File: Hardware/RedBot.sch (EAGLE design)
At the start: 39 parts, among them U2 TB6612FNG, U3 MIC5219 5V

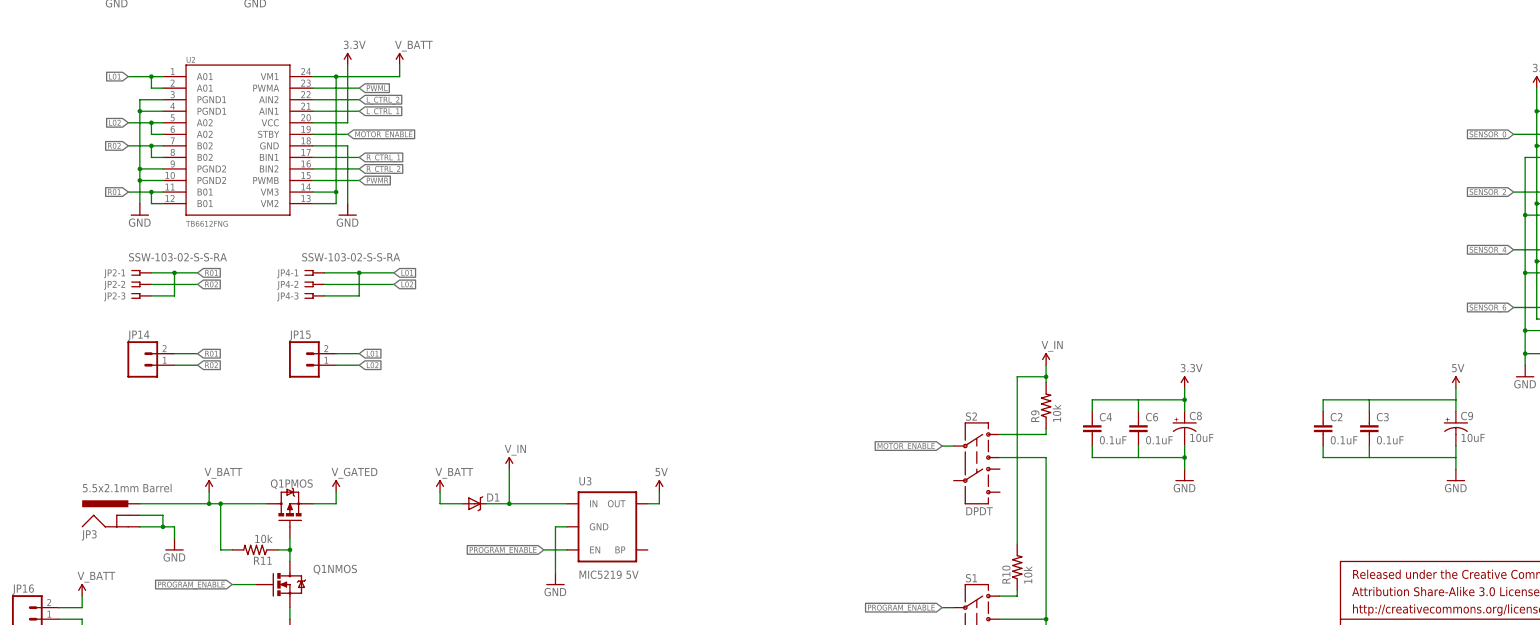
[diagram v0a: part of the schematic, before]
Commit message: Updated board with new power jack. Started routing. Added BOM
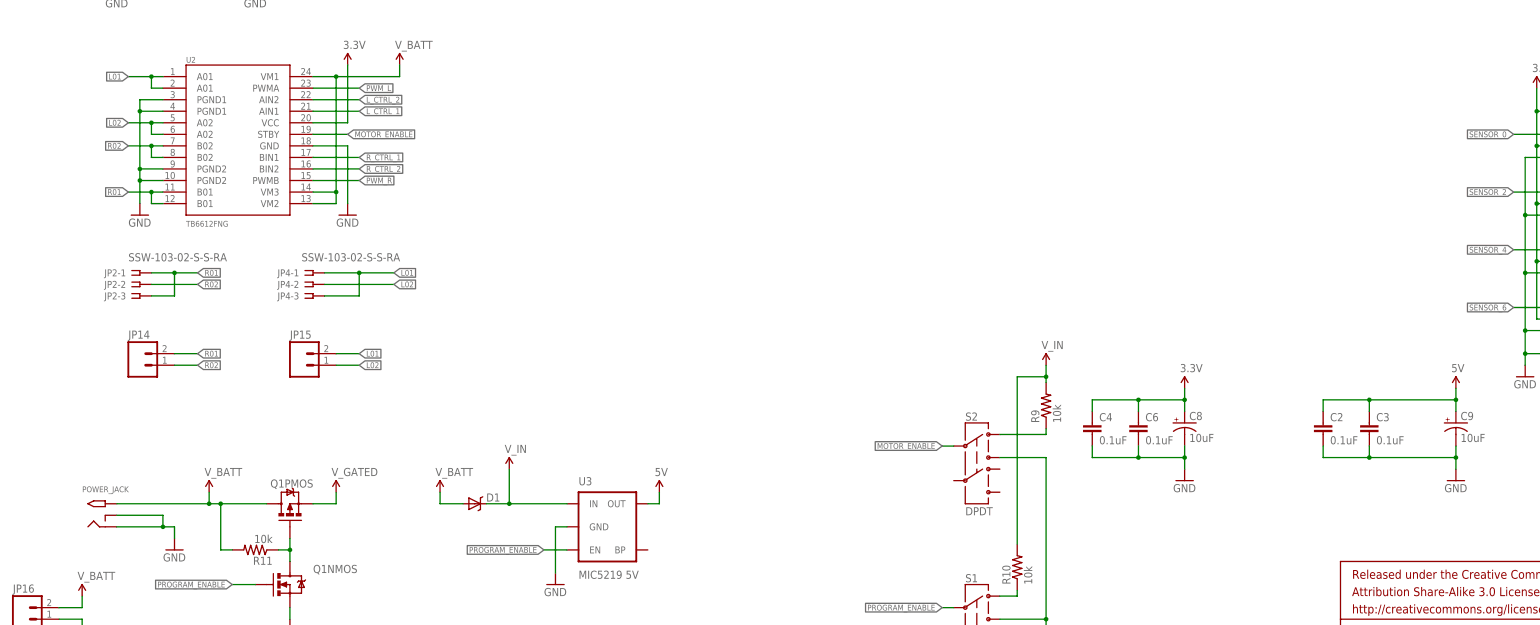
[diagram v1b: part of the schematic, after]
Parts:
- removed JP3: 5.5x2.1mm Barrel, SparkFun-Connectors:POWER_JACKSMD
- added POWER_JACK: 2.1MMJACKTHM, adafruit:2.1MMJACKTHM
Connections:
- removed net PWML: U2.PWMA
- removed net PWMR: U2.PWMB
- net GND: now also POWER_JACK.RING, POWER_JACK.RING_SW; no longer JP3.GND, JP3.GNDBREAK
- net PWM_L: now also U2.PWMA
- net PWM_R: now also U2.PWMB
- net V_BATT: now also POWER_JACK.TIP; no longer JP3.PWR
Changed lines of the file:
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@@
 <setting verticaltext="up"/>
 </settings>
-<grid distance="0.1" unitdist="inch" unit="inch" style="lines" multiple="1" display="no" altdistance="0.01" altunitdist="inch" altunit="inch"/>
+<grid distance="0.05" unitdist="inch" unit="inch" style="lines" multiple="1" display="yes" altdistance="0.005" altunitdist="inch" altunit="inch"/>
 <layers>
 <layer number="1" name="Top" color="4" fill="1" visible="no" active="no"/>
@@
 <layer number="54" name="bGND_GNDA" color="1" fill="9" visible="no" active="no"/>
 <layer number="56" name="wert" color="7" fill="1" visible="no" active="no"/>
+<layer number="57" name="tCAD" color="7" fill="1" visible="no" active="no"/>
 <layer number="59" name="tCarbon" color="7" fill="1" visible="no" active="no"/>
 <layer number="60" name="bCarbon" color="7" fill="1" visible="no" active="no"/>
@@
 <layer number="111" name="Design_Info" color="7" fill="1" visible="yes" active="yes"/>
 <layer number="112" name="CC430_Restrict" color="7" fill="1" visible="yes" active="yes"/>
+<layer number="113" name="IDFDebug" color="4" fill="1" visible="yes" active="yes"/>
 <layer number="116" name="Patch_BOT" color="9" fill="4" visible="no" active="yes"/>
 <layer number="121" name="_tsilk" color="7" fill="1" visible="no" active="yes"/>
@@
 <layer number="125" name="_tNames" color="7" fill="1" visible="no" active="yes"/>
 <layer number="126" name="_bNames" color="7" fill="1" visible="yes" active="yes"/>
+<layer number="127" name="_tValues" color="7" fill="1" visible="yes" active="yes"/>
+<layer number="128" name="_bValues" color="7" fill="1" visible="yes" active="yes"/>
 <layer number="129" name="Mask" color="7" fill="1" visible="yes" active="yes"/>
 <layer number="131" name="tAdjust" color="7" fill="1" visible="yes" active="yes"/>
 <layer number="132" name="bAdjust" color="7" fill="1" visible="yes" active="yes"/>
 <layer number="144" name="Drill_legend" color="7" fill="1" visible="no" active="yes"/>
+<layer number="150" name="Notes" color="7" fill="1" visible="no" active="yes"/>
 <layer number="151" name="HeatSink" color="7" fill="1" visible="no" active="yes"/>
+<layer number="152" name="_bDocu" color="7" fill="1" visible="yes" active="yes"/>
+<layer number="153" name="FabDoc1" color="6" fill="1" visible="no" active="no"/>
+<layer number="154" name="FabDoc2" color="2" fill="1" visible="no" active="no"/>
+<layer number="155" name="FabDoc3" color="7" fill="15" visible="no" active="no"/>
 <layer number="199" name="Contour" color="7" fill="1" visible="yes" active="yes"/>
 <layer number="200" name="200bmp" color="1" fill="10" visible="no" active="yes"/>
@@
 <layer number="223" name="223bmp" color="24" fill="1" visible="no" active="no"/>
 <layer number="224" name="224bmp" color="25" fill="1" visible="no" active="no"/>
+<layer number="248" name="Housing" color="7" fill="1" visible="yes" active="yes"/>
+<layer number="249" name="Edge" color="7" fill="1" visible="yes" active="yes"/>
 <layer number="250" name="Descript" color="3" fill="1" visible="no" active="no"/>
 <layer number="251" name="SMDround" color="12" fill="11" visible="no" active="no"/>
@@
 <part name="C3" library="SparkFun-Capacitors" deviceset="0.1UF-25V(+80/-20%)(0603)" device="" value="0.1uF"/>
 <part name="U2" library="SparkFun-PowerIC" deviceset="TB6621FNG" device="" value="TB6612FNG"/>
-<part name="JP3" library="SparkFun-Connectors" deviceset="POWER_JACK" device="SMD" value="5.5x2.1mm Barrel"/>
 <part name="C4" library="SparkFun-Capacitors" deviceset="0.1UF-25V(+80/-20%)(0603)" device="" value="0.1uF"/>
 <part name="C6" library="SparkFun-Capacitors" deviceset="0.1UF-25V(+80/-20%)(0603)" device="" value="0.1uF"/>
@@
 <part name="JP2" library="con-samtec" deviceset="SSW-103-02-S-S" device="-RA"/>
 <part name="JP4" library="con-samtec" deviceset="SSW-103-02-S-S" device="-RA"/>
+<part name="POWER_JACK" library="adafruit" deviceset="2.1MMJACK" device="THM"/>
 </parts>
 <sheets>
@@
 <instance part="C3" gate="G$1" x="311.15" y="63.5"/>
 <instance part="U2" gate="G$1" x="63.5" y="129.54"/>
-<instance part="JP3" gate="G$1" x="38.1" y="40.64"/>
 <instance part="C4" gate="G$1" x="250.19" y="63.5"/>
 <instance part="C6" gate="G$1" x="260.35" y="63.5"/>
@@
 <instance part="JP4" gate="-2" x="78.74" y="96.52"/>
 <instance part="JP4" gate="-3" x="78.74" y="93.98"/>
+<instance part="POWER_JACK" gate="G$1" x="30.48" y="45.72"/>
 </instances>
 <busses>
@@
 </segment>
 </net>
-<net name="PWML" class="0">
-<segment>
-<pinref part="U2" gate="G$1" pin="PWMA"/>
-<wire x1="78.74" y1="139.7" x2="88.9" y2="139.7" width="0.1524" layer="91"/>
-<label x="88.9" y="139.7" size="1.27" layer="95" xref="yes"/>
-</segment>
-</net>
-<net name="PWMR" class="0">
-<segment>
-<pinref part="U2" gate="G$1" pin="PWMB"/>
-<wire x1="78.74" y1="119.38" x2="88.9" y2="119.38" width="0.1524" layer="91"/>
-<label x="88.9" y="119.38" size="1.27" layer="95" xref="yes"/>
-</segment>
-</net>
 <net name="SERVO_2" class="0">
 <segment>
@@
 <pinref part="GND3" gate="1" pin="GND"/>
 <wire x1="48.26" y1="40.64" x2="48.26" y2="43.18" width="0.1524" layer="91"/>
-<pinref part="JP3" gate="G$1" pin="GND"/>
 <wire x1="48.26" y1="43.18" x2="45.72" y2="43.18" width="0.1524" layer="91"/>
-<wire x1="45.72" y1="43.18" x2="40.64" y2="43.18" width="0.1524" layer="91"/>
-<pinref part="JP3" gate="G$1" pin="GNDBREAK"/>
-<wire x1="40.64" y1="45.72" x2="45.72" y2="45.72" width="0.1524" layer="91"/>
+<wire x1="45.72" y1="43.18" x2="35.56" y2="43.18" width="0.1524" layer="91"/>
+<wire x1="35.56" y1="45.72" x2="45.72" y2="45.72" width="0.1524" layer="91"/>
 <wire x1="45.72" y1="45.72" x2="45.72" y2="43.18" width="0.1524" layer="91"/>
 <junction x="45.72" y="43.18"/>
+<pinref part="POWER_JACK" gate="G$1" pin="RING_SW"/>
+<pinref part="POWER_JACK" gate="G$1" pin="RING"/>
 </segment>
 <segment>
@@
 <wire x1="250.19" y1="60.96" x2="250.19" y2="58.42" width="0.2032" layer="91"/>
 <wire x1="250.19" y1="58.42" x2="260.35" y2="58.42" width="0.2032" layer="91"/>
+<junction x="260.35" y="58.42"/>
 </segment>
 <segment>
@@
 <wire x1="311.15" y1="60.96" x2="311.15" y2="58.42" width="0.1524" layer="91"/>
 <wire x1="311.15" y1="58.42" x2="330.2" y2="58.42" width="0.2032" layer="91"/>
+<junction x="311.15" y="58.42"/>
+<junction x="330.2" y="58.42"/>
 </segment>
 <segment>
@@
 <wire x1="311.15" y1="68.58" x2="311.15" y2="71.12" width="0.1524" layer="91"/>
 <wire x1="311.15" y1="71.12" x2="330.2" y2="71.12" width="0.2032" layer="91"/>
+<junction x="311.15" y="71.12"/>
+<junction x="330.2" y="71.12"/>
 </segment>
 <segment>
@@
 </segment>
 <segment>
-<pinref part="JP3" gate="G$1" pin="PWR"/>
 <pinref part="R11" gate="G$1" pin="2"/>
 <wire x1="60.96" y1="38.1" x2="58.42" y2="38.1" width="0.1524" layer="91"/>
@@
 <wire x1="58.42" y1="48.26" x2="68.58" y2="48.26" width="0.1524" layer="91"/>
 <junction x="58.42" y="48.26"/>
-<wire x1="40.64" y1="48.26" x2="55.88" y2="48.26" width="0.1524" layer="91"/>
+<wire x1="35.56" y1="48.26" x2="55.88" y2="48.26" width="0.1524" layer="91"/>
 <pinref part="U$18" gate="G$1" pin="V_BATT"/>
 <wire x1="55.88" y1="48.26" x2="58.42" y2="48.26" width="0.1524" layer="91"/>
 <wire x1="55.88" y1="50.8" x2="55.88" y2="48.26" width="0.1524" layer="91"/>
 <junction x="55.88" y="48.26"/>
+<pinref part="POWER_JACK" gate="G$1" pin="TIP"/>
 </segment>
 <segment>
@@
 <wire x1="250.19" y1="68.58" x2="250.19" y2="71.12" width="0.2032" layer="91"/>
 <wire x1="250.19" y1="71.12" x2="260.35" y2="71.12" width="0.2032" layer="91"/>
+<junction x="260.35" y="71.12"/>
 </segment>
 <segment>
@@
 <label x="393.7" y="238.76" size="1.27" layer="95" xref="yes"/>
 </segment>
+<segment>
+<pinref part="U2" gate="G$1" pin="PWMA"/>
+<wire x1="78.74" y1="139.7" x2="88.9" y2="139.7" width="0.1524" layer="91"/>
+<label x="88.9" y="139.7" size="1.27" layer="95" xref="yes"/>
+</segment>
 </net>
 <net name="PWM_R" class="0">
@@
 <label x="393.7" y="236.22" size="1.27" layer="95" xref="yes"/>
 </segment>
-</net>
+<segment>
+<pinref part="U2" gate="G$1" pin="PWMB"/>
+<wire x1="78.74" y1="119.38" x2="88.9" y2="119.38" width="0.1524" layer="91"/>
+<label x="88.9" y="119.38" size="1.27" layer="95" xref="yes"/>
+</segment>
+</net>

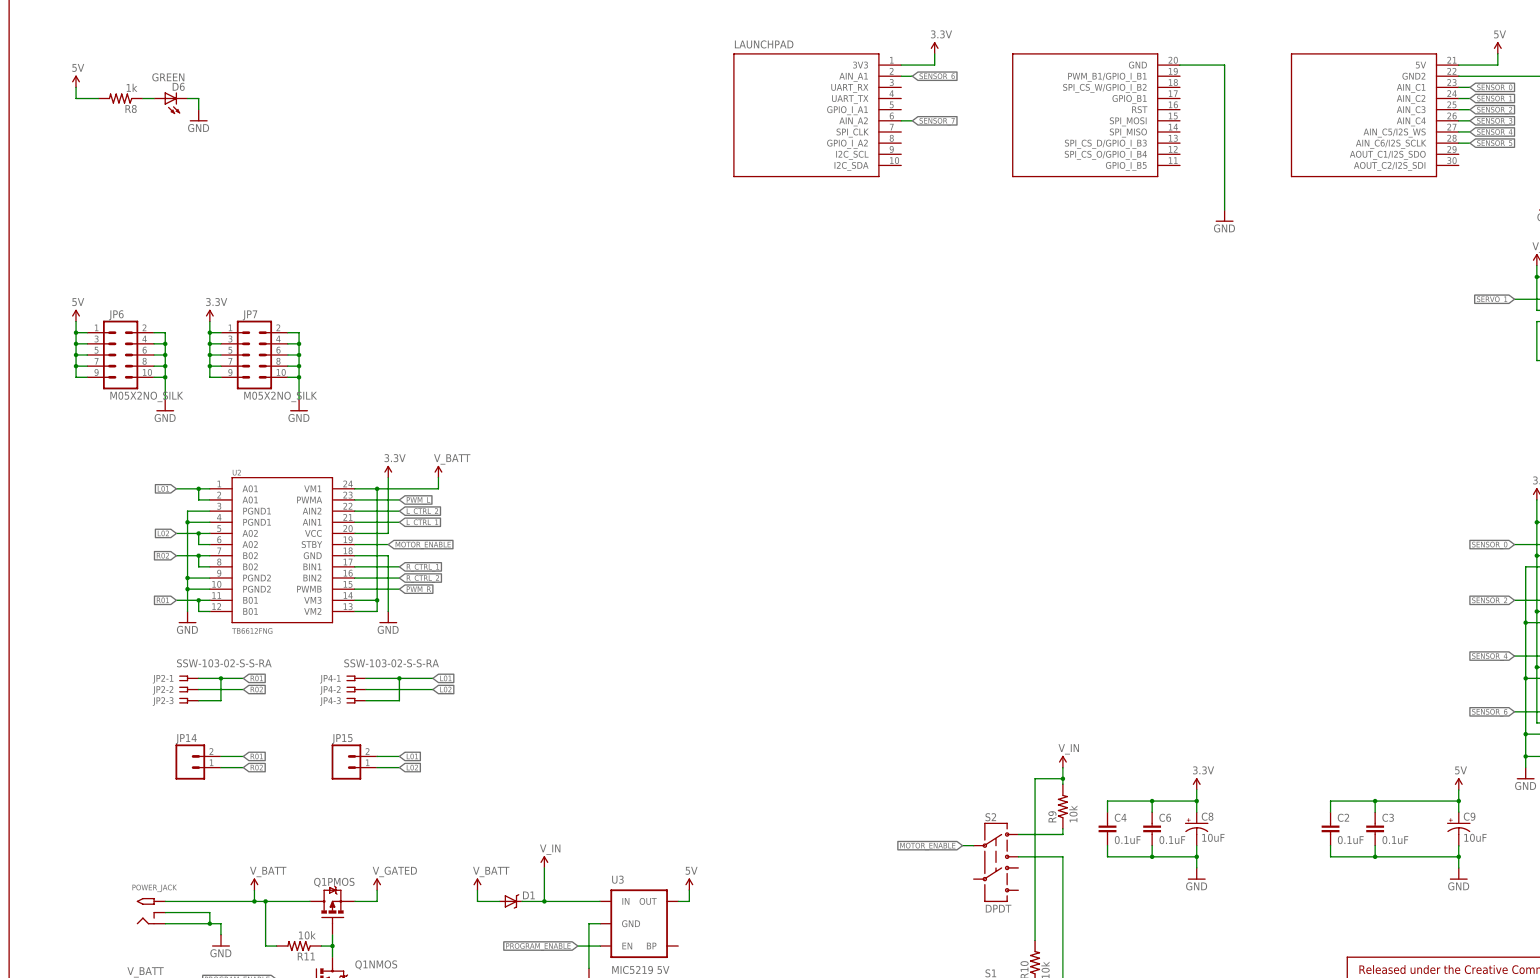
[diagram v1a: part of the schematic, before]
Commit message: Updated all parts to be larger
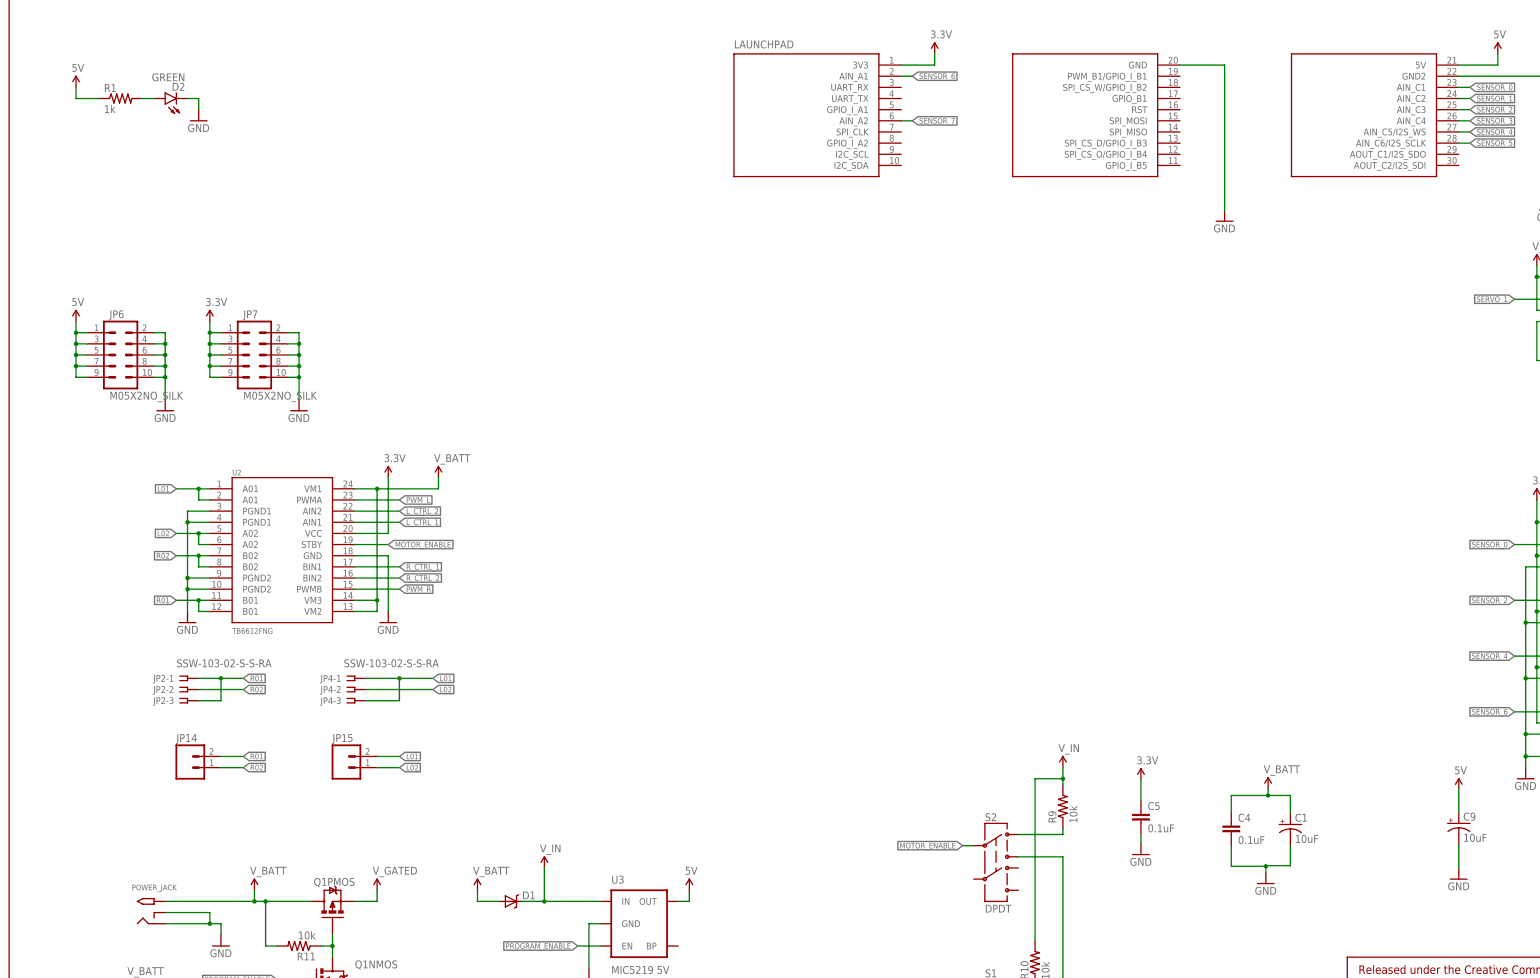
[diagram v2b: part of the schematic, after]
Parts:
- removed C2, C3, C6: 0.1uF, SparkFun-Capacitors:0.1UF-25V(+80/-20%)(0603)
- removed C8: 10uF, SparkFun-Capacitors:10UF-16V-10%(TANT)
- removed D6: GREEN, SparkFun-LED:LED-GREEN0603
- removed R8: 1k, SparkFun-Resistors:1K-1%
- added C1: 10uF, SparkFun-Capacitors:10UF-16V-10%(TANT)
- added C5: 0.1uF, SparkFun-Capacitors:CAP1206
- added D2: GREEN, SparkFun-LED:LED-GREENLARGE
- added R1: 1k, SparkFun-Resistors:RESISTOR1206
- C4: device SparkFun-Capacitors:0.1UF-25V(+80/-20%)(0603) -> SparkFun-Capacitors:CAP1206
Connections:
- removed net N$8: D6.A, R8.1
- new net N$1: D2.A, R1.2
- net 3.3V: now also C5.1; no longer C4.1, C6.1, C8.+
- net 5V: now also R1.1; no longer C2.1, C3.1, R8.2
- net GND: now also C1.-, C5.2, D2.C; no longer C2.2, C3.2, C6.2, C8.-, D6.C
- net V_BATT: now also C1.+, C4.1
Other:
- moved on the sheet: C4

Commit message: Finished layout of RedBot
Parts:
- R10, R11, R9: device SparkFun-Resistors:10KOHM1/10W1%(0603)0603 -> SparkFun-Resistors:RESISTOR1206; PROD_ID RES-00824 -> (none)
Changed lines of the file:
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@@
 <part name="U$13" library="SparkFun-Aesthetics" deviceset="5V" device=""/>
 <part name="V_IN1" library="SparkFun-Aesthetics" deviceset="5V" device="" value="V_IN"/>
-<part name="R9" library="SparkFun-Resistors" deviceset="10KOHM1/10W1%(0603)" device="0603" value="10k">
-<attribute name="PROD_ID" value="RES-00824"/>
-</part>
-<part name="R10" library="SparkFun-Resistors" deviceset="10KOHM1/10W1%(0603)" device="0603" value="10k">
-<attribute name="PROD_ID" value="RES-00824"/>
-</part>
+<part name="R9" library="SparkFun-Resistors" deviceset="RESISTOR" device="1206" value="10k"/>
+<part name="R10" library="SparkFun-Resistors" deviceset="RESISTOR" device="1206" value="10k"/>
 <part name="JP6" library="SparkFun-Connectors" deviceset="M05X2" device="NO_SILK" value="M05X2NO_SILK"/>
 <part name="JP7" library="SparkFun-Connectors" deviceset="M05X2" device="NO_SILK" value="M05X2NO_SILK"/>
@@
 <part name="Q1" library="SparkFun-DiscreteSemi" deviceset="IRF7509" device=""/>
 <part name="GND19" library="SparkFun-Aesthetics" deviceset="GND" device=""/>
-<part name="R11" library="SparkFun-Resistors" deviceset="10KOHM1/10W1%(0603)" device="0603" value="10k">
-<attribute name="PROD_ID" value="RES-00824"/>
-</part>
+<part name="R11" library="SparkFun-Resistors" deviceset="RESISTOR" device="1206" value="10k"/>
 <part name="U$18" library="SparkFun-Aesthetics" deviceset="V_BATT" device=""/>
 <part name="GND20" library="SparkFun-Aesthetics" deviceset="GND" device=""/>
